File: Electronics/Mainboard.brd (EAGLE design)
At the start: 68.6 x 53.3 mm, 12 parts

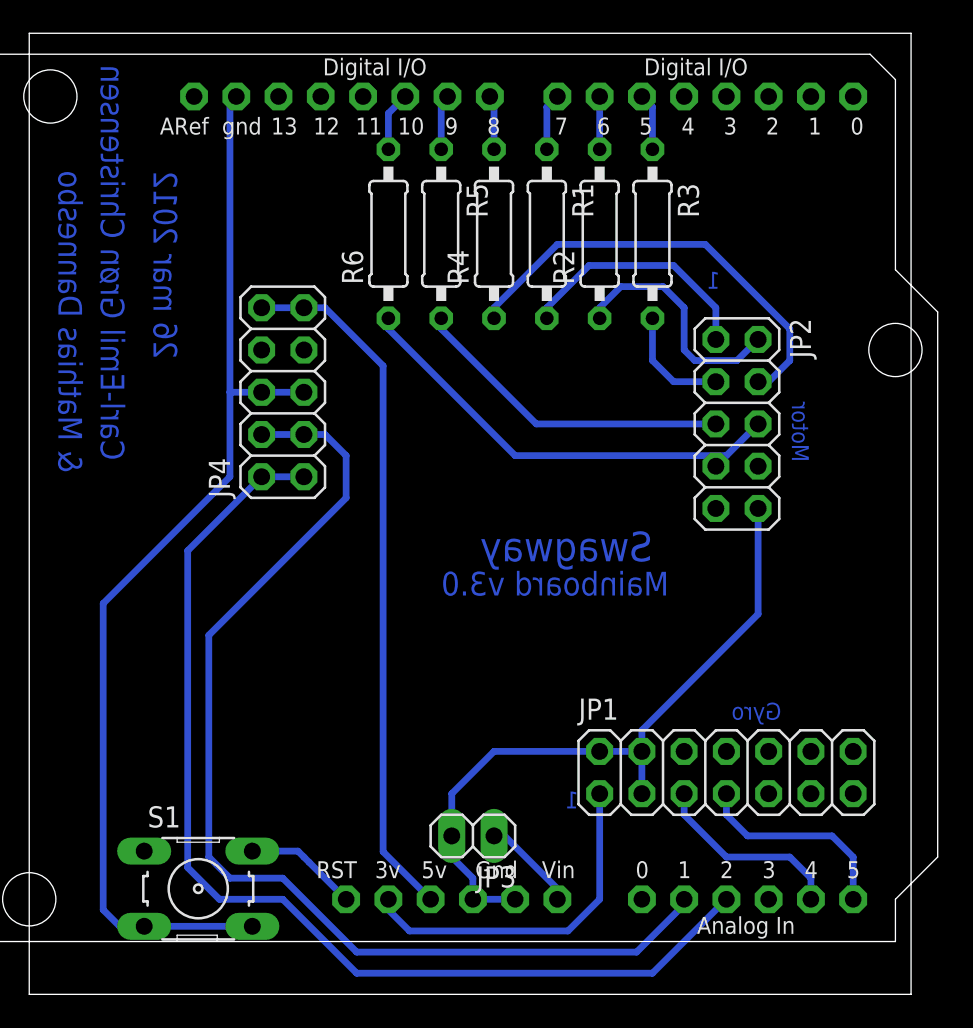
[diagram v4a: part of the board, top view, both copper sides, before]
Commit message: Radio on mainboard. Closes #29
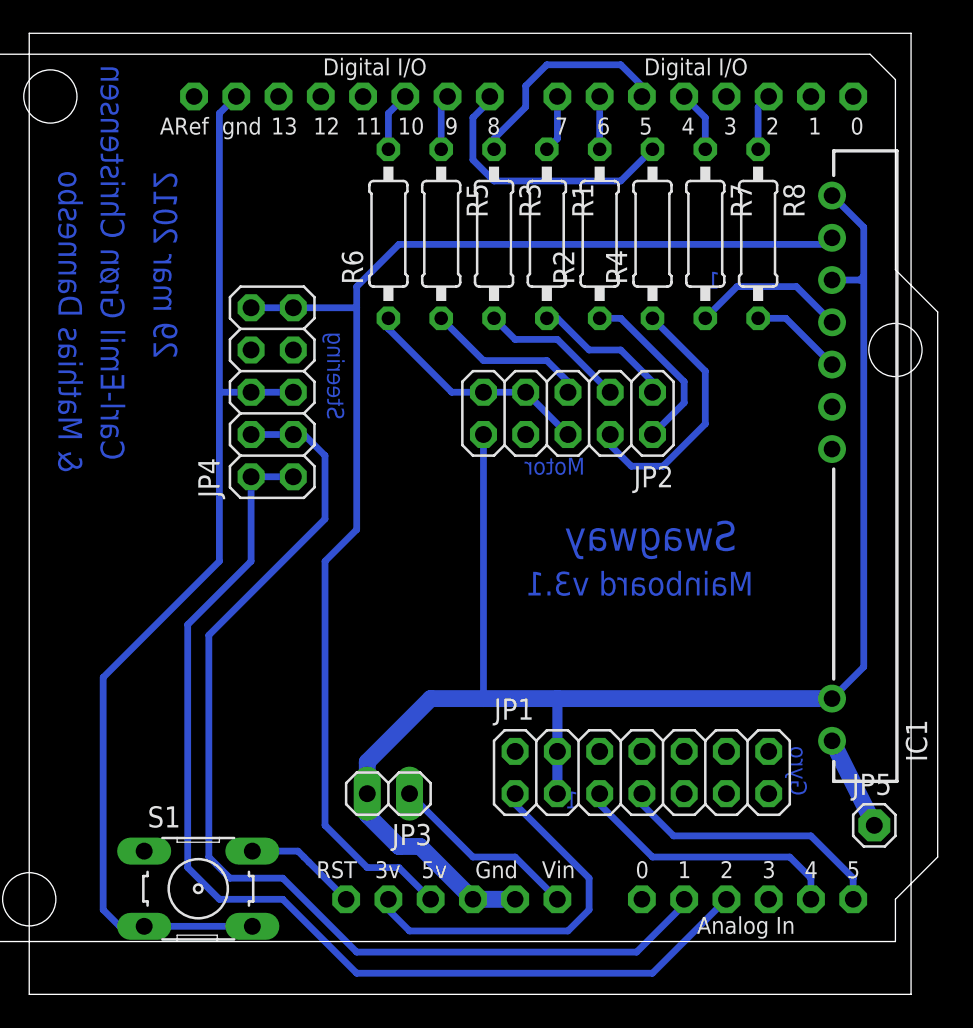
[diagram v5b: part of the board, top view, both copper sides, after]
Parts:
- added IC1: ER400RTS-02, lprs:SIL9
- added JP5: (no value), adafruit:1X01
- added R7, R8: 10k, rcl:0207/10
- moved JP2 10.2 mm to (32.4, 31.8), turned to 180 degrees
- moved R3 9.53 mm to (27.9, 42.5)
- moved R4 9.53 mm to (37.5, 42.5)
- moved JP3 5.68 mm to (21.6, 8.89)
- moved JP1 5.08 mm to (36.8, 10.2)
- moved JP4 0.63 mm to (14.6, 33.0)
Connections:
- new net N$12: R7.1, U$1.D4
- new net N$18: IC1.5, R8.2
- new net N$19: IC1.6, R7.2
- new net N$21: IC1.1, JP5.1
- new net N$9: R8.1, U$1.D2
- net +5V: now also IC1.8
- net GND: now also IC1.2, IC1.7, IC1.9
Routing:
- net GND: track 108.0 -> 165.1 mm
- net +5V: track 42.0 -> 77.5 mm
- net N$11: track 3.28 -> 16.3 mm
- net N$6: track 26.8 -> 14.1 mm
- net N$5: track 26.4 -> 15.6 mm
- net N$8: track 3.44 -> 13.3 mm
- net N$3: track 19.5 -> 9.83 mm
- net N$19: track 0.00 -> 9.30 mm
- net N$1: track 14.8 -> 8.56 mm
- net N$39: track 5.76 -> 11.5 mm
- net N$21: track 0.00 -> 5.68 mm
- net N$18: track 0.00 -> 5.60 mm
- net N$41: track 11.7 -> 16.4 mm
- net N$26: track 12.5 -> 16.4 mm
- net N$4: track 14.5 -> 10.6 mm
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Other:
- board text added: "29 mar 2012"
- board text added: "Mainboard v3.1"
- board text added: "Steering"
- board text removed: "26 mar 2012"
- board text removed: "Mainboard v3.0"

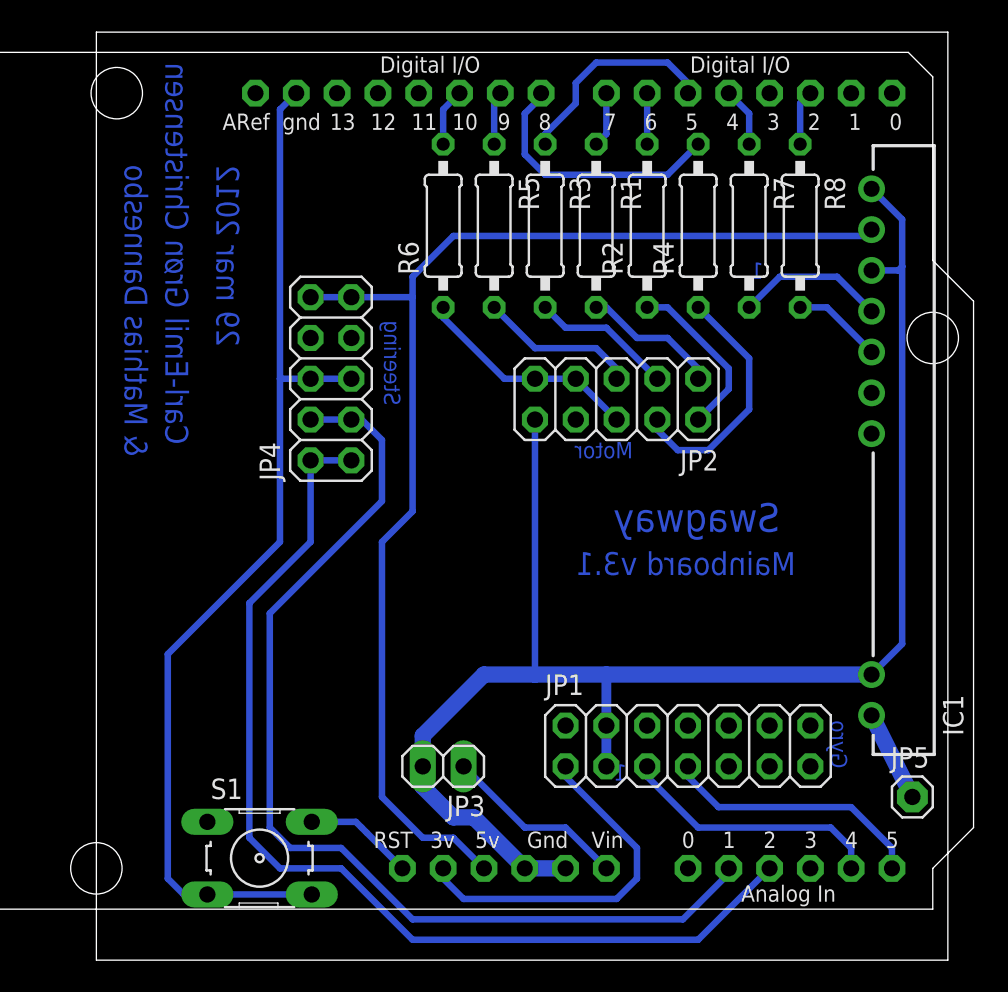
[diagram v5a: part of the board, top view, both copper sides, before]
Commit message: Moved resistors to Motorboard. Closes #37
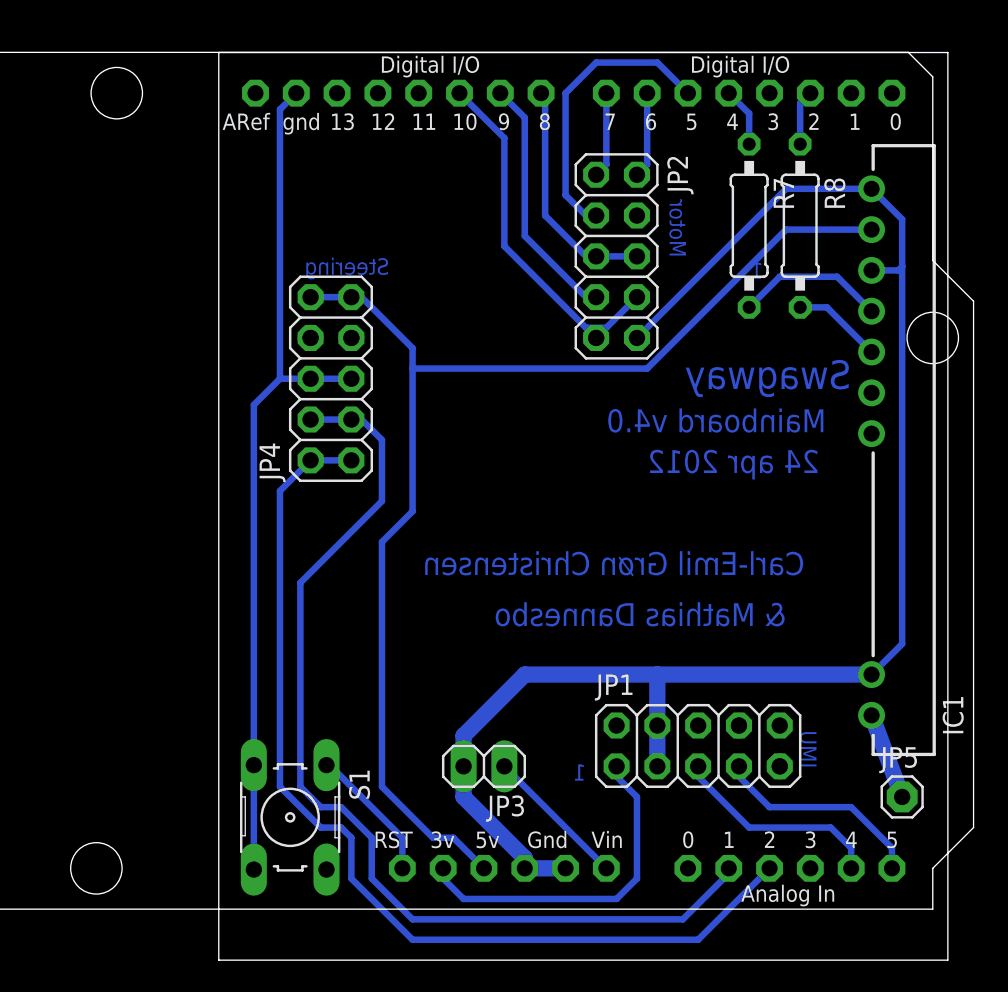
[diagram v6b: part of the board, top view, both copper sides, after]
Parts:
- removed R1, R2, R3, R4, R5, R6: 330R, rcl:0207/10
- JP1: value Gyro -> IMU; device pinhead:2X07 -> pinhead:2X05
- moved JP2 8.89 mm to (32.4, 40.6), turned to 270 degrees
- moved S1 3.17 mm to (12.1, 5.71), turned to 270 degrees
- moved JP3 2.54 mm to (24.1, 8.89)
- moved JP1 0.64 mm to (37.5, 10.2)
- moved JP5 0.63 mm to (50.2, 6.99)
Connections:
- removed net N$10: R2.2, U$1.D6
- removed net N$11: R4.2, U$1.D8
- removed net N$17: R6.2, U$1.D10
- removed net N$2: JP2.3, R3.2
- removed net N$3: JP2.5, R5.2
- removed net N$7: R1.1, U$1.D7
- net N$1: now also U$1.D7; no longer R1.2
- net N$15: now also S1.1; no longer S1.2
- net N$16: now also JP2.7; no longer R5.1
- net N$4: now also U$1.D6; no longer R2.1
- net N$5: now also JP2.6, U$1.D8; no longer JP2.4, R4.1
- net N$6: now also JP2.8, U$1.D10; no longer JP2.6, R6.1
- net N$8: now also JP2.3; no longer R3.1
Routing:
- net N$11: track 16.3 -> 0.00 mm, vias 0 -> 1
- net GND: track 165.1 -> 151.2 mm
- net N$16: track 3.33 -> 15.5 mm
- net N$3: track 9.83 -> 0.00 mm, vias 0 -> 1
- net N$2: track 8.83 -> 0.00 mm, vias 0 -> 1
- net N$6: track 14.1 -> 21.8 mm
- net N$4: track 10.6 -> 5.34 mm
- net N$8: track 13.3 -> 18.0 mm
- net N$17: track 3.60 -> 0.00 mm
- net N$7: track 3.44 -> 0.00 mm, vias 0 -> 1
- net N$1: track 8.56 -> 5.34 mm
- net N$41: track 16.4 -> 13.3 mm
- net N$26: track 16.4 -> 13.3 mm
- net N$10: track 3.17 -> 0.00 mm, vias 0 -> 1
- net N$14: track 64.5 -> 61.4 mm
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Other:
- board text added: "24 apr 2012"
- board text added: "IMU"
- board text added: "Mainboard v4.0"
- board text removed: "29 mar 2012"
- board text removed: "Gyro"
- board text removed: "Mainboard v3.1"
